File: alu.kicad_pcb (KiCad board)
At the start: 2 copper layers, 100 x 100 mm, 64 parts, among them J0 640-USB4970-00-A, Q0 DMG2302U-7, Q1 DMG2302U-7, Q2 DMG2302U-7, Q3 DMG2302U-7, Q4 DMG2302U-7, Q5 DMG2302U-7, SW0 418127270904, SW1 418127270904, SW2 418127270904, U0 SN74LS08N, U1 SN74HC86N, U10 SN74LVC1G32DBVR, U11 SN74LS08N, U12 SN74LS08N, U13 CD74HCT32E, U14 CD74HCT32E, U2 SN74HC86N, U3 SN74LS08N, U4 SN74LS08N, U5 CD74HCT32E, U6 SN74LS08N, U7 SN74LS08N, U8 SN74HC86N, U9 SN74LS08N

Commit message: fix: fixed ground issue
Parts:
- turned R0 to 90 degrees
- turned R4 to 90 degrees
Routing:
- net Net-(Q3-D): track 9.35 -> 51.1 mm, vias 0 -> 1
- net GND: track 36.0 -> 0.94 mm, vias 1 -> 0
- net IN_A0: track 36.7 -> 33.5 mm
- net IN_A2: track 30.0 -> 28.5 mm
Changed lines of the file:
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@@
 	(footprint "Resistor_SMD:R_0603_1608Metric_Pad0.98x0.95mm_HandSolder"
 		(layer "F.Cu")
-		(at 69.38 78.9125 -90)
+		(at 69.38 78.9125 90)
 		(descr "Resistor SMD 0603 (1608 Metric), square (rectangular) end terminal, IPC-7351 nominal with elongated pad for handsoldering. (Body size source: IPC-SM-782 page 72, https://www.pcb-3d.com/wordpress/wp-content/uploads/ipc-sm-782a_amendment_1_and_2.pdf)")
 		(tags "resistor handsolder")
@@
 		(duplicate_pad_numbers_are_jumpers no)
 		(fp_line
-			(start -0.254724 0.5225)
-			(end 0.254724 0.5225)
+			(start -0.254724 -0.5225)
+			(end 0.254724 -0.5225)
 			(stroke
 				(width 0.12)
@@
 		)
 		(fp_line
-			(start -0.254724 -0.5225)
-			(end 0.254724 -0.5225)
+			(start -0.254724 0.5225)
+			(end 0.254724 0.5225)
 			(stroke
 				(width 0.12)
@@
 		)
 		(pad "1" smd roundrect
-			(at -0.9125 0 270)
+			(at -0.9125 0 90)
 			(size 0.975 0.95)
 			(layers "F.Cu" "F.Mask" "F.Paste")
@@
 		)
 		(pad "2" smd roundrect
-			(at 0.9125 0 270)
+			(at 0.9125 0 90)
 			(size 0.975 0.95)
 			(layers "F.Cu" "F.Mask" "F.Paste")
@@
 	(footprint "Resistor_SMD:R_0603_1608Metric_Pad0.98x0.95mm_HandSolder"
 		(layer "F.Cu")
-		(at 69.545 87.4575 -90)
+		(at 69.545 87.4575 90)
 		(descr "Resistor SMD 0603 (1608 Metric), square (rectangular) end terminal, IPC-7351 nominal with elongated pad for handsoldering. (Body size source: IPC-SM-782 page 72, https://www.pcb-3d.com/wordpress/wp-content/uploads/ipc-sm-782a_amendment_1_and_2.pdf)")
 		(tags "resistor handsolder")
@@
 		(duplicate_pad_numbers_are_jumpers no)
 		(fp_line
-			(start -0.254724 0.5225)
-			(end 0.254724 0.5225)
+			(start -0.254724 -0.5225)
+			(end 0.254724 -0.5225)
 			(stroke
 				(width 0.12)
@@
 		)
 		(fp_line
-			(start -0.254724 -0.5225)
-			(end 0.254724 -0.5225)
+			(start -0.254724 0.5225)
+			(end 0.254724 0.5225)
 			(stroke
 				(width 0.12)
@@
 		)
 		(pad "1" smd roundrect
-			(at -0.9125 0 270)
+			(at -0.9125 0 90)
 			(size 0.975 0.95)
 			(layers "F.Cu" "F.Mask" "F.Paste")
@@
 		)
 		(pad "2" smd roundrect
-			(at 0.9125 0 270)
+			(at 0.9125 0 90)
 			(size 0.975 0.95)
 			(layers "F.Cu" "F.Mask" "F.Paste")
@@
 	)
 	(segment
-		(start 127.005 76.5)
-		(end 127.395 76.11)
+		(start 71.1 92.4)
+		(end 71.0425 92.4575)
 		(width 0.2)
 		(layer "F.Cu")
 		(net "GND")
 	)
-	(via
-		(at 73.9125 118.8)
-		(size 0.6)
-		(drill 0.3)
-		(layers "F.Cu" "B.Cu")
-		(net "GND")
-	)
 	(segment
-		(start 73.9125 118.8)
-		(end 73.0625 117.95)
+		(start 69.285 84.54)
+		(end 69.5 84.325)
 		(width 0.2)
-		(layer "B.Cu")
+		(layer "F.Cu")
 		(net "GND")
 	)
 	(segment
-		(start 73.0625 117.95)
-		(end 73.0625 83.7)
+		(start 127.005 76.5)
+		(end 127.395 76.11)
 		(width 0.2)
-		(layer "B.Cu")
+		(layer "F.Cu")
 		(net "GND")
 	)
@@
 	)
 	(segment
-		(start 84.12 87.65)
-		(end 84.27 87.8)
-		(width 0.2)
-		(layer "F.Cu")
-		(net "IN_A1")
-	)
-	(segment
-		(start 69.5 82.5)
-		(end 68.66 82.5)
+		(start 68.66 82.5)
+		(end 69.5 82.5)
 		(width 0.2)
 		(layer "F.Cu")
@@
 	)
 	(segment
-		(start 68.66 82.5)
-		(end 66.62 84.54)
+		(start 84.12 87.65)
+		(end 84.27 87.8)
 		(width 0.2)
 		(layer "F.Cu")
@@
 	)
 	(segment
+		(start 66.62 84.54)
+		(end 68.66 82.5)
+		(width 0.2)
+		(layer "F.Cu")
+		(net "IN_A1")
+	)
+	(segment
 		(start 84.27 90.06)
 		(end 84.36 90.15)
@@
 	)
 	(segment
-		(start 79.28 100.92)
+		(start 73 101)
 		(end 79.2 101)
 		(width 0.2)
@@
 	)
 	(segment
-		(start 73 101)
-		(end 73 87.4)
+		(start 69.545 88.37)
+		(end 70.82 88.37)
 		(width 0.2)
 		(layer "F.Cu")
@@
 	)
 	(segment
-		(start 79.2 101)
-		(end 73 101)
+		(start 79.28 100.92)
+		(end 79.28 97.77)
 		(width 0.2)
 		(layer "F.Cu")
@@
 	)
 	(segment
-		(start 72.145 86.545)
-		(end 69.545 86.545)
+		(start 73 90.55)
+		(end 73 101)
 		(width 0.2)
 		(layer "F.Cu")
@@
 	)
 	(segment
-		(start 69.545 86.545)
-		(end 67.155 86.545)
+		(start 67.155 86.545)
+		(end 66.62 87.08)
 		(width 0.2)
 		(layer "F.Cu")
@@
 	)
 	(segment
-		(start 73 87.4)
-		(end 72.145 86.545)
+		(start 68.07 88.37)
+		(end 69.545 88.37)
 		(width 0.2)
 		(layer "F.Cu")
@@
 	)
 	(segment
-		(start 67.155 86.545)
-		(end 66.62 87.08)
+		(start 66.78 87.08)
+		(end 68.07 88.37)
 		(width 0.2)
 		(layer "F.Cu")
@@
 	)
 	(segment
-		(start 79.28 97.77)
+		(start 79.2 101)
 		(end 79.28 100.92)
 		(width 0.2)
@@
 	)
 	(segment
+		(start 70.82 88.37)
+		(end 73 90.55)
+		(width 0.2)
+		(layer "F.Cu")
+		(net "IN_A2")
+	)
+	(segment
+		(start 66.62 87.08)
+		(end 66.78 87.08)
+		(width 0.2)
+		(layer "F.Cu")
+		(net "IN_A2")
+	)
+	(segment
 		(start 72.5 84.65)
 		(end 72.765 84.915)
@@
 	)
 	(segment
-		(start 69.38 78)
-		(end 66.62 80.76)
+		(start 72.5 80.75)
+		(end 72.45 80.75)
 		(width 0.2)
 		(layer "F.Cu")
@@
 	)
 	(segment
-		(start 72.5 78)
+		(start 71.525 79.825)
+		(end 69.38 79.825)
+		(width 0.2)
+		(layer "F.Cu")
+		(net "IN_A0")
+	)
+	(segment
+		(start 72.45 80.75)
+		(end 71.525 79.825)
+		(width 0.2)
+		(layer "F.Cu")
+		(net "IN_A0")
+	)
+	(segment
+		(start 72.5 80.75)
 		(end 72.5 84.65)
 		(width 0.2)
@@
 	)
 	(segment
+		(start 66.62 80.76)
+		(end 67.555 79.825)
+		(width 0.2)
+		(layer "F.Cu")
+		(net "IN_A0")
+	)
+	(segment
 		(start 72.765 84.915)
 		(end 76.65 84.915)
@@
 	)
 	(segment
-		(start 69.38 78)
-		(end 72.5 78)
+		(start 67.555 79.825)
+		(end 69.38 79.825)
 		(width 0.2)
 		(layer "F.Cu")
@@
 	)
 	(segment
+		(start 73.15 119.8)
+		(end 73.15 120.75)
+		(width 0.2)
+		(layer "F.Cu")
+		(net "Net-(Q3-D)")
+	)
+	(segment
+		(start 73.15 120.75)
+		(end 73.55 121.15)
+		(width 0.2)
+		(layer "F.Cu")
+		(net "Net-(Q3-D)")
+	)
+	(via
+		(at 73.55 121.15)
+		(size 0.6)
+		(drill 0.3)
+		(layers "F.Cu" "B.Cu")
+		(net "Net-(Q3-D)")
+	)
+	(segment
+		(start 79.025 80)
+		(end 75 80)
+		(width 0.2)
+		(layer "B.Cu")
+		(net "Net-(Q3-D)")
+	)
+	(segment
+		(start 74.1 120.6)
+		(end 73.55 121.15)
+		(width 0.2)
+		(layer "B.Cu")
+		(net "Net-(Q3-D)")
+	)
+	(segment
 		(start 79.025 80)
 		(end 81.73 77.295)
@@
 	)
 	(segment
-		(start 73.5 80)
-		(end 79.025 80)
+		(start 75 80)
+		(end 74.1 80.9)
+		(width 0.2)
+		(layer "B.Cu")
+		(net "Net-(Q3-D)")
+	)
+	(segment
+		(start 74.1 80.9)
+		(end 74.1 120.6)
 		(width 0.2)
 		(layer "B.Cu")

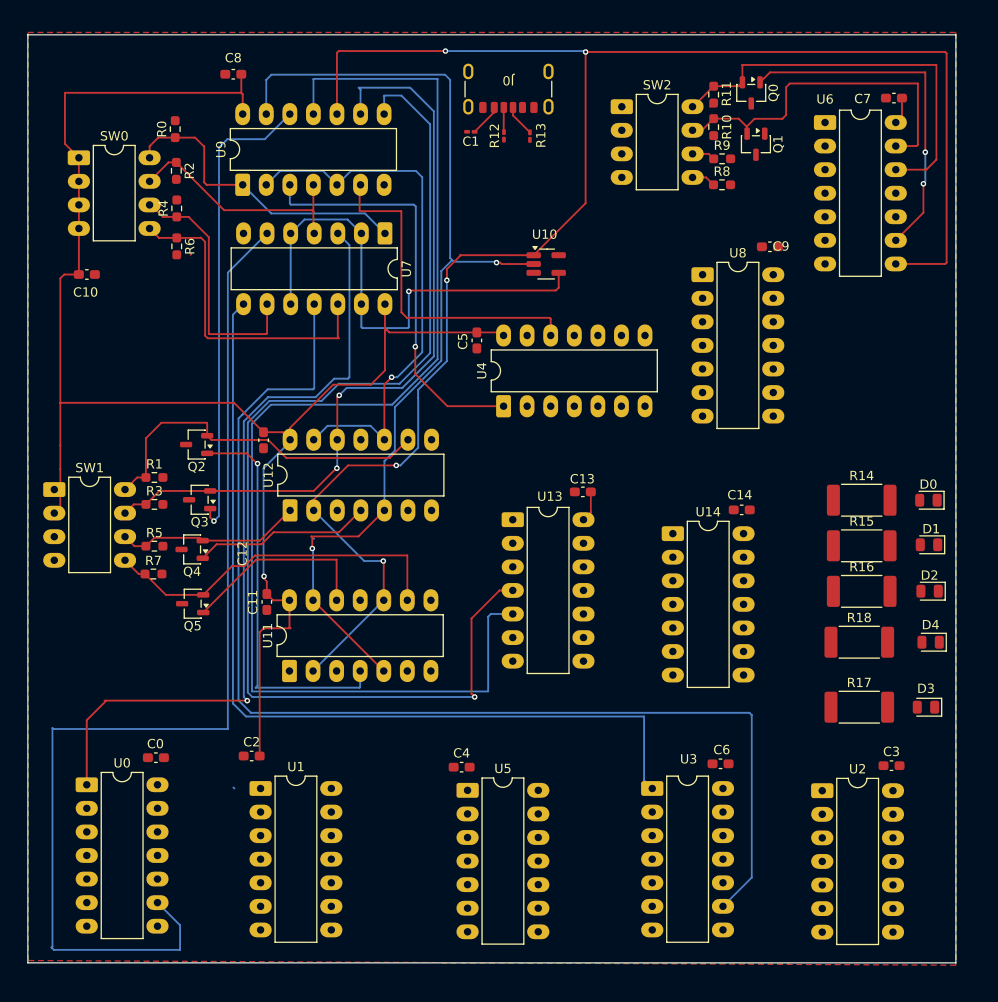
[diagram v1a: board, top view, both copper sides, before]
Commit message: Routed bottom part of the PCB
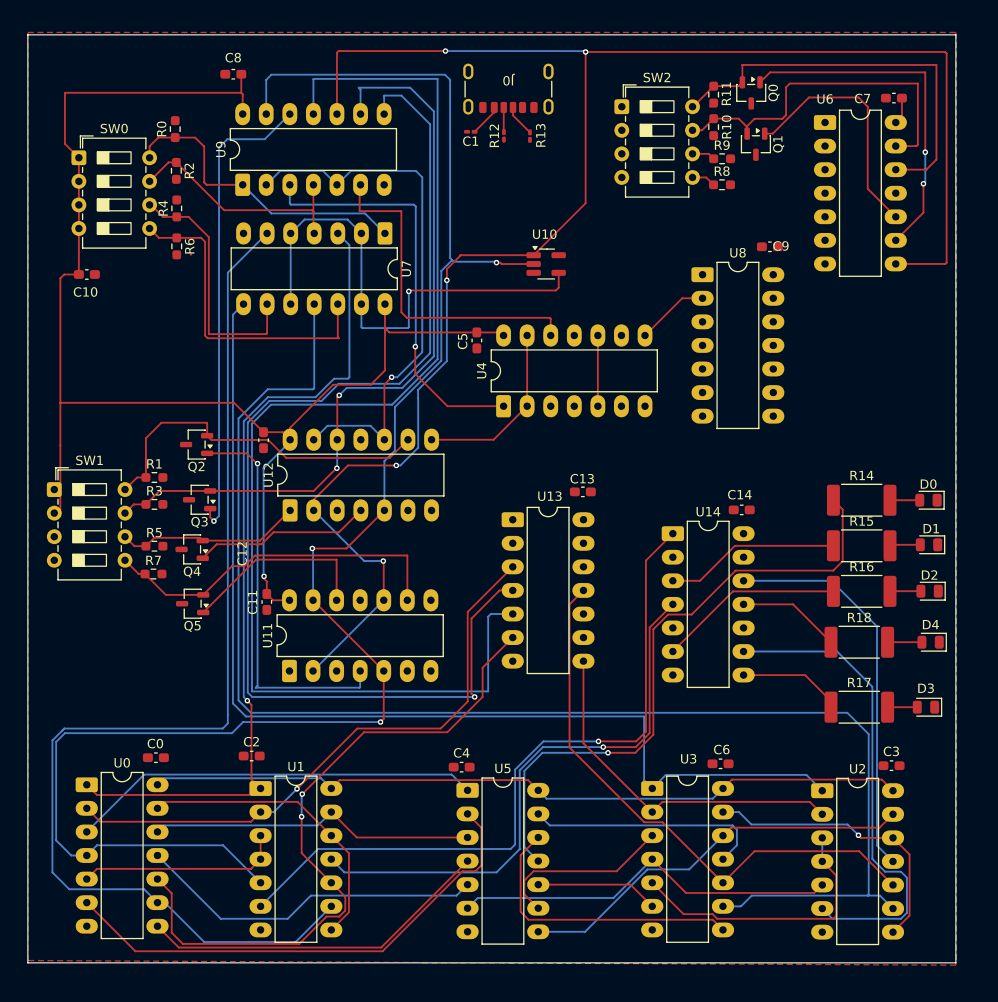
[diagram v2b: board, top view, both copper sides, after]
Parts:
- SW0, SW1, SW2: footprint Package_DIP:DIP-8_W7.62mm_LongPads -> Button_Switch_THT:SW_DIP_SPSTx04_Slide_6.7x11.72mm_W7.62mm_P2.54mm_LowProfile
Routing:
- net OUT_ADD_0: track 0.00 -> 76.6 mm, vias 0 -> 1
- net SUB: track 109.2 -> 185.2 mm, vias 2 -> 3
- net OUT_SEL_ADD_B1: track 0.00 -> 73.1 mm, vias 0 -> 2
- net ADD_OVERFLOW: track 0.00 -> 67.6 mm, vias 0 -> 1
- net OUT_SEL_ADD_B0: track 0.00 -> 63.5 mm, vias 0 -> 1
- net OUT_SEL_ADD_B3: track 0.00 -> 61.3 mm
- net OUT_ADD_1: track 0.00 -> 61.0 mm, vias 0 -> 1
- net +5V: track 183.9 -> 243.2 mm
- net Net-(U0-Pad6): track 0.00 -> 54.7 mm
- net OUT_ADD_2: track 0.00 -> 52.2 mm
- net Net-(U0-Pad3): track 0.00 -> 44.5 mm
- net /1-bit-adder2/C_OUT: track 0.00 -> 43.5 mm
- net OUT_ADD_3: track 0.00 -> 42.5 mm
- net /1-bit-adder1/C_OUT: track 0.00 -> 42.3 mm
- net OUT_SEL_ADD_B2: track 0.00 -> 38.7 mm
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
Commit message: feat: all connected, 30+ errors remaining
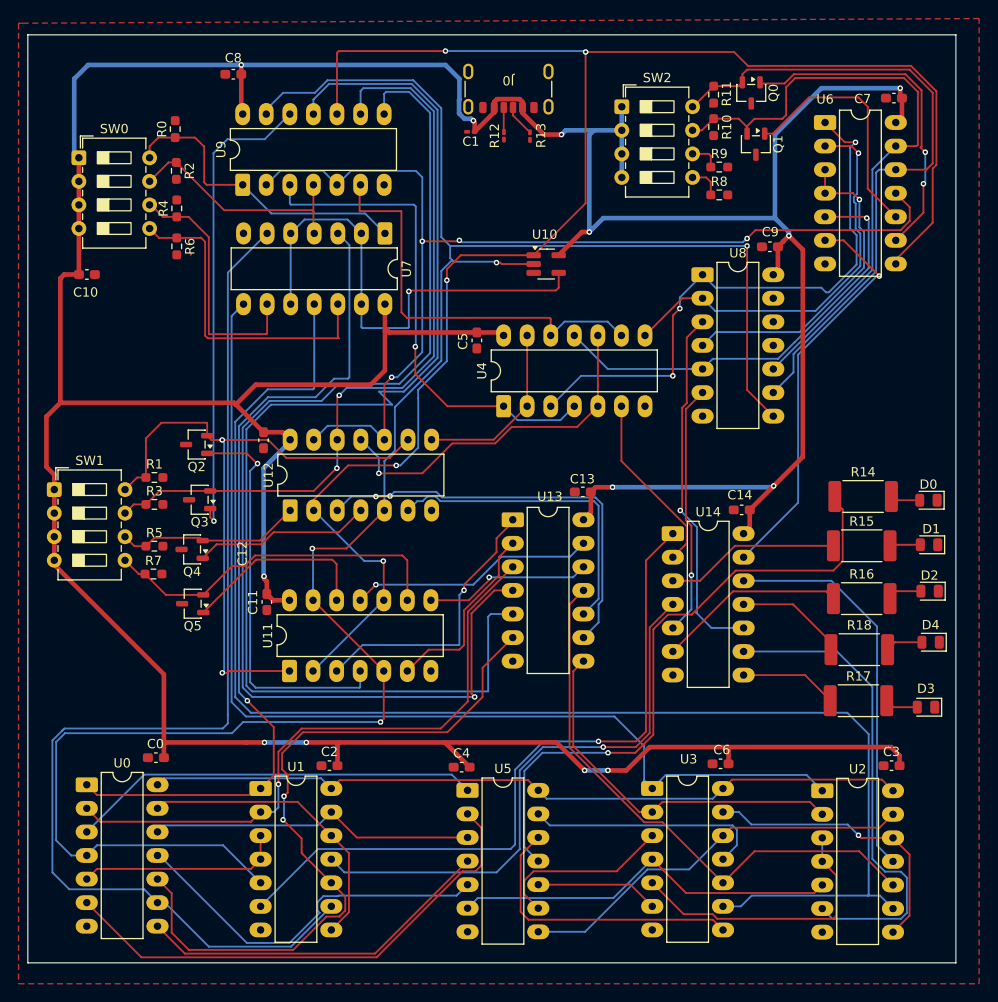
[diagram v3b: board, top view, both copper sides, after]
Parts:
- moved C2 8.45 mm to (86.0, 147.5)
- moved R8 1.13 mm to (128.0, 86.0)
- moved R9 0.94 mm to (128.0, 83.0)
- moved R18 0.80 mm to (143.1, 135.0)
- moved R16 0.78 mm to (143.3, 129.5)
- moved R17 0.71 mm to (143.0, 140.5)
- moved R14 0.43 mm to (143.5, 118.5)
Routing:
- net +5V: track 243.2 -> 555.3 mm, vias 1 -> 13
- net Net-(U4-Pad3): track 0.00 -> 63.2 mm, vias 0 -> 3
- net MUL: track 58.3 -> 115.5 mm, vias 1 -> 4
- net Net-(U4-Pad11): track 0.00 -> 47.8 mm, vias 0 -> 1
- net SUB: track 185.2 -> 232.0 mm, vias 3 -> 4
- net Net-(U12-Pad3): track 0.00 -> 45.1 mm, vias 0 -> 2
- net OUT_MUL_3: track 0.00 -> 44.0 mm, vias 0 -> 1
- net OUT_MUL_2: track 0.00 -> 39.0 mm, vias 0 -> 1
- net Net-(U4-Pad8): track 7.86 -> 44.0 mm, vias 0 -> 1
- net Net-(U6-Pad3): track 0.00 -> 34.9 mm, vias 0 -> 1
- net Net-(U12-Pad6): track 0.00 -> 33.9 mm
- net IN_B0: track 39.1 -> 72.1 mm, vias 0 -> 2
- net OUT_SEL_MUL_B1: track 7.62 -> 38.6 mm, vias 0 -> 1
- net Net-(U11-Pad3): track 0.00 -> 30.3 mm, vias 0 -> 1
- net /binary-decoder/IN_OP2: track 39.4 -> 68.8 mm
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
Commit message: Remove capacitors + change R and C footprints + finish PCB routing
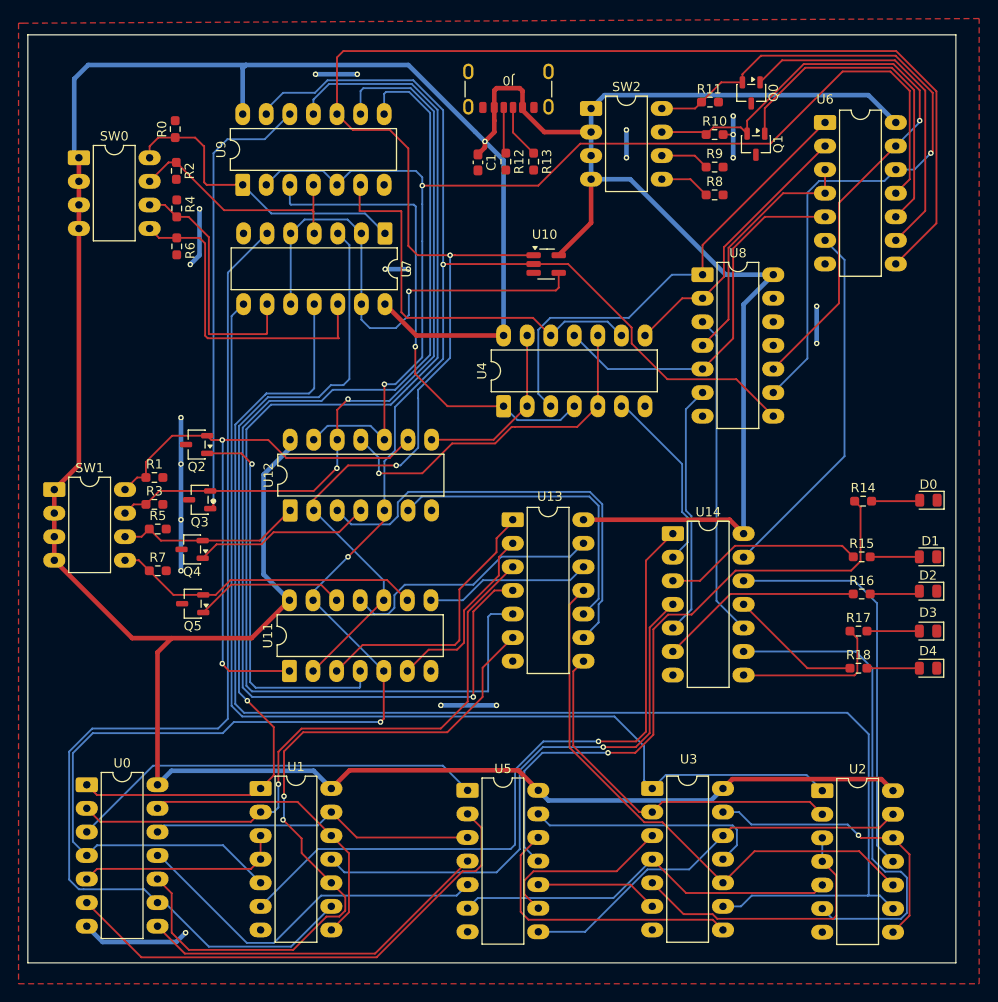
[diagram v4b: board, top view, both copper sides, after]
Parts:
- removed C0, C10, C11, C12, C13, C14, C2, C3, C4, C5, C6, C7, C8, C9: CC0603KRX7R9BB104, Capacitor_SMD:C_0603_1608Metric_Pad1.08x0.95mm_HandSolder
- C1: footprint Capacitor_SMD:C_0201_0603Metric_Pad0.64x0.40mm_HandSolder -> Capacitor_SMD:C_0603_1608Metric_Pad1.08x0.95mm_HandSolder
- R12, R13: footprint Resistor_SMD:R_0201_0603Metric_Pad0.64x0.40mm_HandSolder -> Resistor_SMD:R_0603_1608Metric_Pad0.98x0.95mm_HandSolder
- R14, R15, R16, R17, R18: footprint Resistor_SMD:R_2512_6332Metric_Pad1.40x3.35mm_HandSolder -> Resistor_SMD:R_0603_1608Metric_Pad0.98x0.95mm_HandSolder
- SW0, SW1, SW2: footprint Button_Switch_THT:SW_DIP_SPSTx04_Slide_6.7x11.72mm_W7.62mm_P2.54mm_LowProfile -> Package_DIP:DIP-8_W7.62mm_LongPads
- moved D3 8.20 mm to (150.5, 133.0)
- moved R17 7.50 mm to (143.0, 133.0)
- moved C1 3.39 mm to (102.0, 82.5), turned to -90 degrees
- moved SW2 3.32 mm to (114.2, 76.7)
- moved D4 2.81 mm to (150.5, 137.0)
- moved R12 2.79 mm to (105.0, 82.4)
- moved R13 2.77 mm to (108.0, 82.4)
- moved R18 2.00 mm to (143.0, 137.0)
- moved R5 1.89 mm to (67.5, 122.0)
- moved D1 1.30 mm to (150.5, 125.0)
- moved R15 1.19 mm to (143.3, 125.0)
- moved R11 0.89 mm to (127.0, 76.0), turned to 0 degrees
- moved R10 0.81 mm to (127.5, 79.5), turned to 0 degrees
- moved R7 0.58 mm to (67.5, 126.5)
- moved R14 0.50 mm to (143.5, 119.0)
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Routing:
- net +5V: track 555.3 -> 440.0 mm, vias 13 -> 1
- net GND: track 0.94 -> 60.6 mm, vias 0 -> 20
- net SUB: track 232.0 -> 207.7 mm, vias 4 -> 3
- net Net-(U4-Pad8): track 44.0 -> 29.7 mm, vias 1 -> 0
- net MUL: track 115.5 -> 128.6 mm, vias 4 -> 2
- net Net-(U4-Pad3): track 63.2 -> 50.8 mm, vias 3 -> 0
- net Net-(Q1-D): track 26.2 -> 36.1 mm
- net Net-(U6-Pad3): track 34.9 -> 27.1 mm, vias 1 -> 0
- net /binary-decoder/IN_OP1: track 71.5 -> 78.4 mm, vias 0 -> 1
- net Net-(U4-Pad11): track 47.8 -> 41.0 mm, vias 1 -> 0
- net /collector/OUT_2: track 10.5 -> 17.2 mm
- net IN_B3: track 38.2 -> 33.5 mm
- net OUT_SEL_ADD_A1: track 124.2 -> 119.4 mm
- net Net-(Q5-D): track 20.8 -> 16.3 mm
- net OUT_MUL_3: track 44.0 -> 39.5 mm, vias 1 -> 0
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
